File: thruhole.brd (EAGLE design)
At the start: 35.6 x 50.8 mm, 12 parts

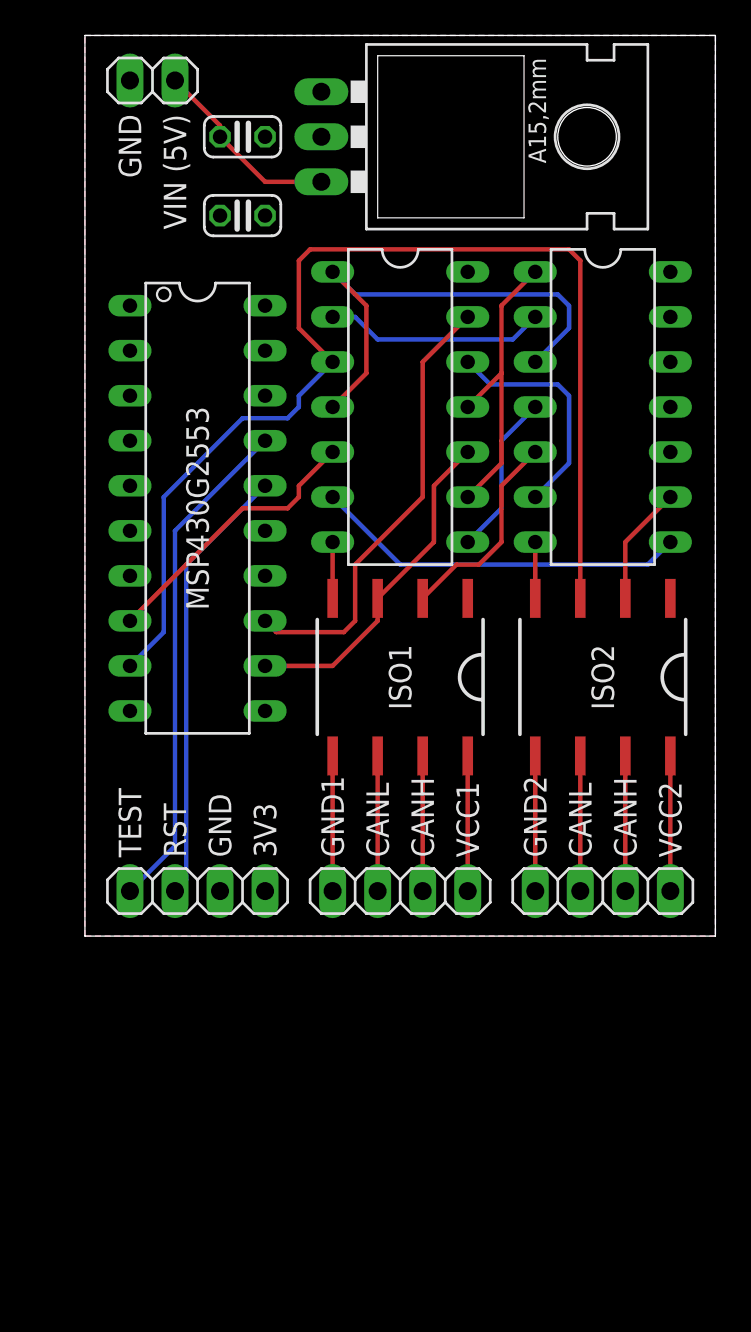
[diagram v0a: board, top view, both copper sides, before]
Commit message: Moved components on thruhole board closer together and swapped pin headers for 1x12 pin header
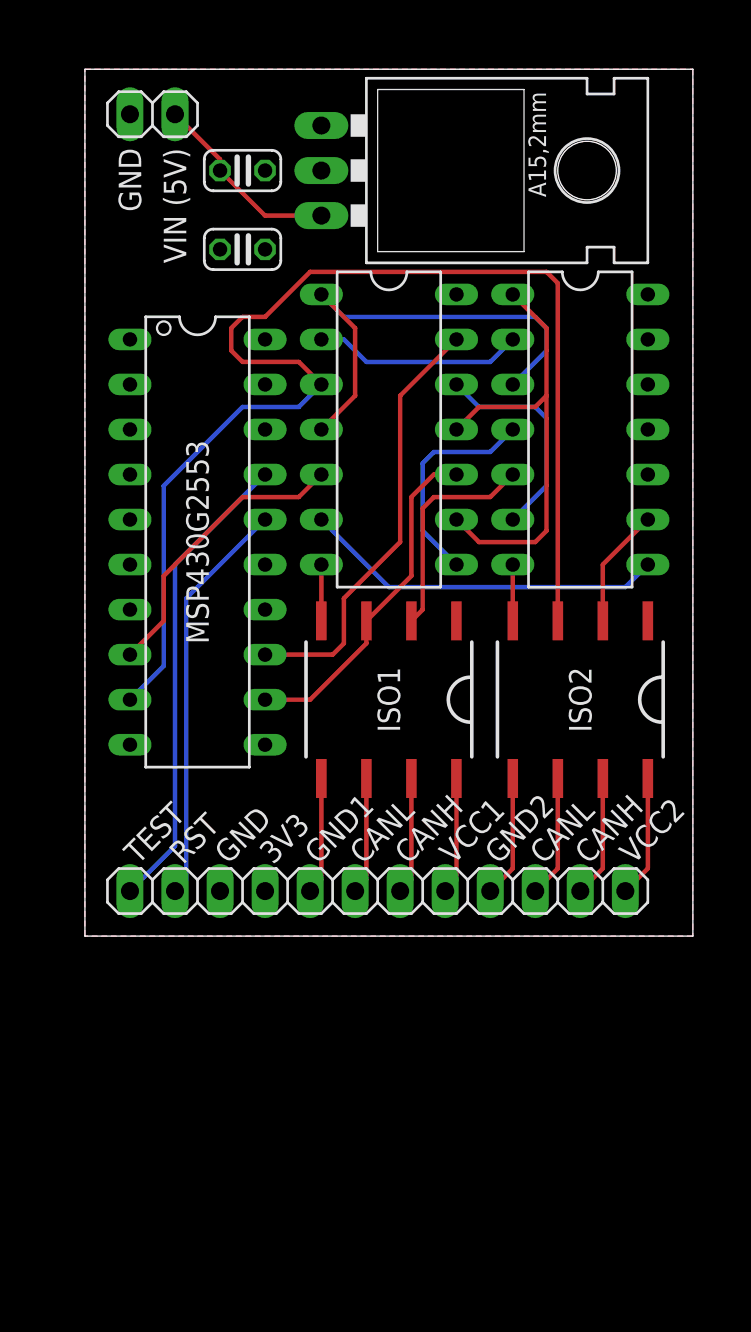
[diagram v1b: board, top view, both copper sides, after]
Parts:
- removed CAN1, CAN2, ICSP: (no value), pinhead:1X04
- added JP1: (no value), pinhead:1X12
- moved C1 1.91 mm to (8.89, 43.2)
- moved C2 1.91 mm to (8.89, 38.7)
- moved LD117AV33 1.91 mm to (17.1, 43.2)
- moved VIN 1.91 mm to (3.81, 46.4)
- moved MSP430G2553 1.90 mm to (6.35, 22.2)
- moved INV 1.80 mm to (27.9, 28.6)
- moved ISO2 1.80 mm to (27.9, 13.3)
- moved ISO1 1.42 mm to (17.1, 13.3)
- moved NAND 1.42 mm to (17.1, 28.6)
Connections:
- net GND: now also JP1.3; no longer ICSP.2
- net N$1: now also JP1.2; no longer ICSP.3
- net N$10: now also JP1.11; no longer CAN2.2
- net N$11: now also JP1.10; no longer CAN2.3
- net N$12: now also JP1.9; no longer CAN2.4
- net N$13: now also JP1.8; no longer CAN1.1
- net N$14: now also JP1.7; no longer CAN1.2
- net N$15: now also JP1.6; no longer CAN1.3
- net N$16: now also JP1.5; no longer CAN1.4
- net N$2: now also JP1.1; no longer ICSP.4
- net N$9: now also JP1.12; no longer CAN2.1
- net VCC: now also JP1.4; no longer ICSP.1
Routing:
- net N$7: track 17.0 -> 25.9 mm
- net N$24: track 65.3 -> 70.3 mm
- net N$5: track 9.20 -> 12.4 mm
- net N$2: track 28.6 -> 26.7 mm
- net N$1: track 25.0 -> 23.1 mm
- net N$14: track 7.62 -> 6.61 mm
- net N$13: track 7.62 -> 6.61 mm
- net N$15: track 7.62 -> 6.61 mm
- net N$16: track 7.62 -> 6.61 mm
- net N$22: track 25.4 -> 24.5 mm
- net N$18: track 11.6 -> 12.5 mm
- net N$9: track 7.62 -> 6.88 mm
- net N$21: track 15.7 -> 16.5 mm
- net N$12: track 7.62 -> 6.88 mm
- net N$10: track 7.62 -> 6.88 mm
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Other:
- board size 35.6 x 50.8 mm -> 34.3 x 48.9 mm

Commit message: Separated thruhole 1x12 pin header into 3 1x4 pin headers for rules compliance
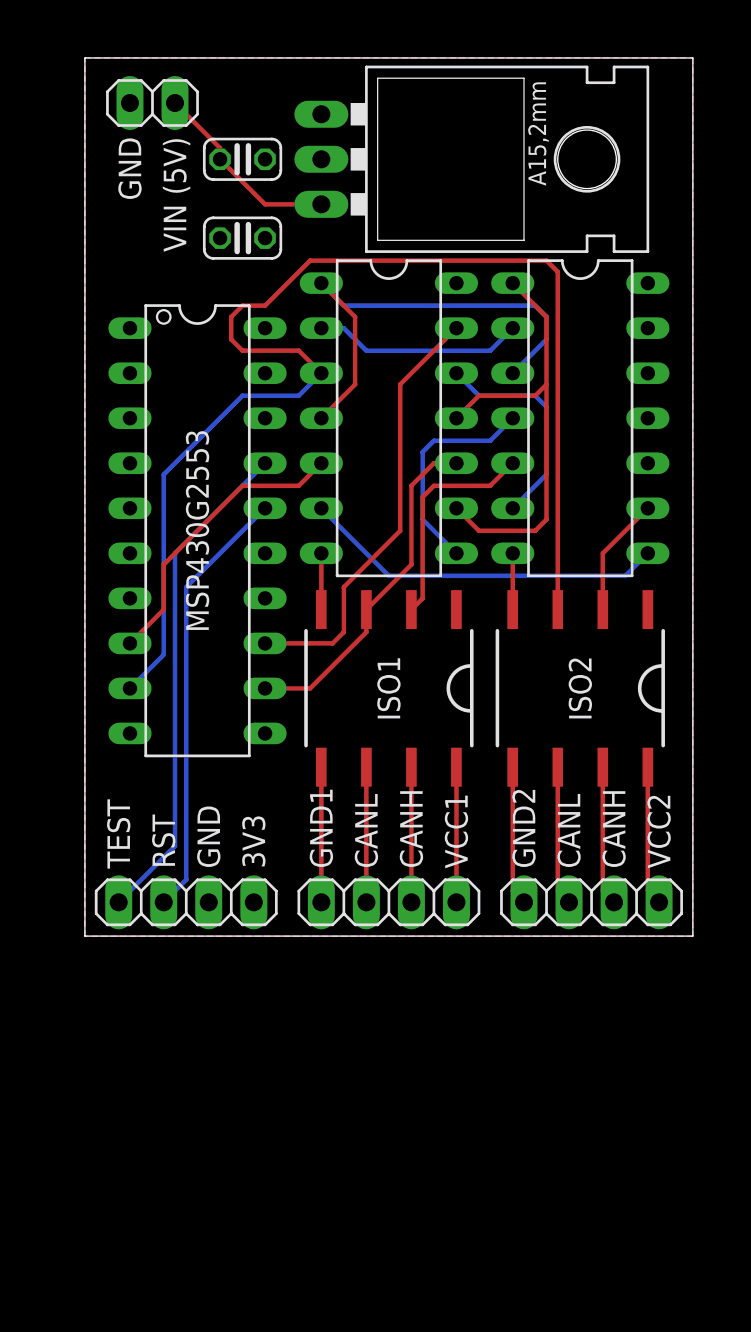
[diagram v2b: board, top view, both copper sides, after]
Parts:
- added JP2, JP3: (no value), pinhead:1X04
- JP1: device pinhead:1X12 -> pinhead:1X04
- moved JP1 10.8 mm to (5.71, 1.91)
- moved VIN 0.64 mm to (3.81, 47.0)
- moved INV 0.64 mm to (27.9, 29.2)
- moved NAND 0.64 mm to (17.1, 29.2)
- moved ISO1 0.63 mm to (17.1, 14.0)
- moved ISO2 0.63 mm to (27.9, 14.0)
- moved C1 0.63 mm to (8.89, 43.8)
- moved C2 0.63 mm to (8.89, 39.4)
- moved LD117AV33 0.63 mm to (17.1, 43.8)
- moved MSP430G2553 0.63 mm to (6.35, 22.9)
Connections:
- net N$10: now also JP3.3; no longer JP1.11
- net N$11: now also JP3.2; no longer JP1.10
- net N$12: now also JP3.1; no longer JP1.9
- net N$13: now also JP2.4; no longer JP1.8
- net N$14: now also JP2.3; no longer JP1.7
- net N$15: now also JP2.2; no longer JP1.6
- net N$16: now also JP2.1; no longer JP1.5
- net N$9: now also JP3.4; no longer JP1.12
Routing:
- net N$2: track 26.7 -> 28.2 mm
- net N$1: track 23.1 -> 24.6 mm
- net N$12: track 6.88 -> 7.88 mm
- net N$14: track 6.61 -> 7.62 mm
- net N$13: track 6.61 -> 7.62 mm
- net N$15: track 6.61 -> 7.62 mm
- net N$9: track 6.88 -> 7.88 mm
- net N$16: track 6.61 -> 7.62 mm
- net N$10: track 6.88 -> 7.88 mm
- net N$11: track 6.88 -> 7.88 mm
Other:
- board size 34.3 x 48.9 mm -> 34.3 x 49.5 mm

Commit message: WIP: Added 555 timer to thruhole board
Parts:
- added IC1: LM555N, linear:DIL08
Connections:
- new net V+: IC1.8
- net GND: now also IC1.1
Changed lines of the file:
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@@
 <attribute name="VALUE" x="23.495" y="-1.27" size="1.27" layer="27"/>
 </element>
+<element name="IC1" library="linear" package="DIL08" value="LM555N" x="4.445" y="-15.875"/>
 </elements>
 <signals>
@@
 <wire x1="13.335" y1="18.415" x2="13.335" y2="21.59" width="0.254" layer="1"/>
 <contactref element="JP1" pad="3"/>
+<contactref element="IC1" pad="1"/>
+<wire x1="6.985" y1="1.905" x2="0.635" y2="-19.685" width="0" layer="19" extent="1-1"/>
 </signal>
 <signal name="N$1">
@@
 <wire x1="19.685" y1="26.67" x2="18.415" y2="25.4" width="0.254" layer="1"/>
 </signal>
+<signal name="V+">
+<contactref element="IC1" pad="8"/>
+</signal>
 </signals>
